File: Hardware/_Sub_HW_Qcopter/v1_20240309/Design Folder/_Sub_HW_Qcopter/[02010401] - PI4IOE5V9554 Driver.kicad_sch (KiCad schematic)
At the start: 2 parts, among them U1001 PI4IOE5V9554ZHEX

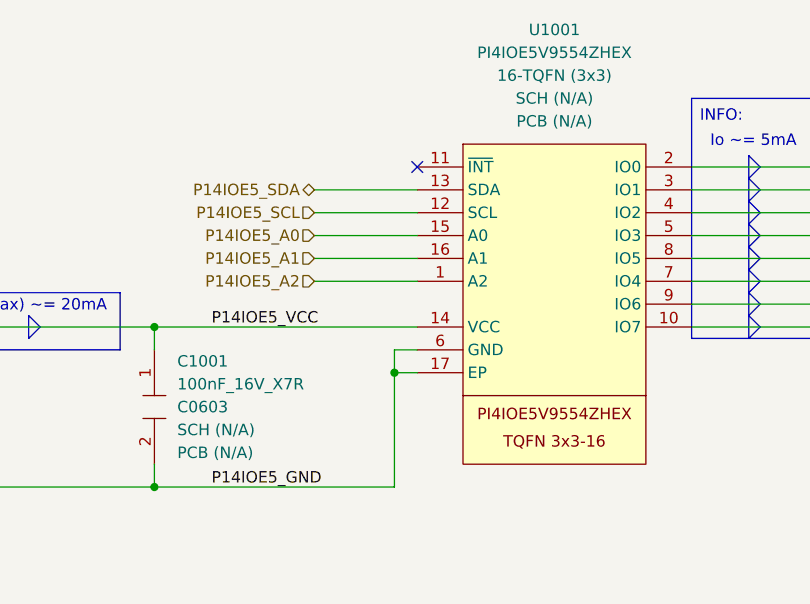
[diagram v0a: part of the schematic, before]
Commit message: Update [02010401] - PI4IOE5V9554 Driver.kicad_sch
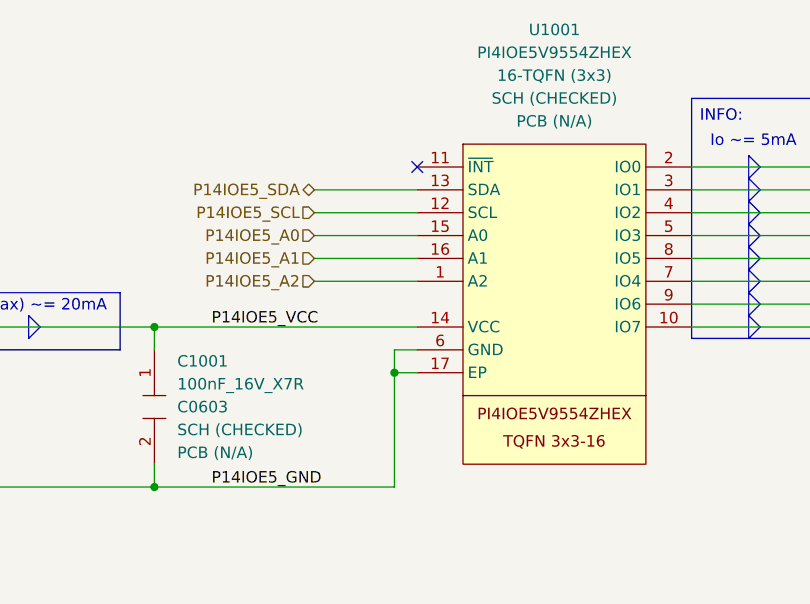
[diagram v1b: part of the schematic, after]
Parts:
- C1001, U1001: SCH CHECK SCH (N/A) -> SCH (CHECKED)
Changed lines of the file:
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@@
 			)
 		)
-		(property "SCH CHECK" "SCH (N/A)"
+		(property "SCH CHECK" "SCH (CHECKED)"
 			(at 217.17 212.0899 90)
 			(effects
@@
 			)
 		)
-		(property "SCH CHECK" "SCH (N/A)"
+		(property "SCH CHECK" "SCH (CHECKED)"
 			(at 259.08 175.26 0)
 			(effects
